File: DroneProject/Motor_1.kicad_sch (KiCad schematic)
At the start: 0 parts

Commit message: Added a second MCU for motor control.  Removed 5V rail.  Added COM switching for SWD and UART external headers
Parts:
- added C1: 10uF, Capacitor_SMD:C_1206_3216Metric, symbol Device:C
- added C2, C3: 0.1uF, Capacitor_SMD:C_0402_1005Metric, symbol Device:C
- added C4, C81: 1uF, Capacitor_SMD:C_0402_1005Metric, symbol Device:C
- added C82: 47nF, Capacitor_SMD:C_0402_1005Metric, symbol Device:C
- added U91: DRV8323SRTAR, Library:RTA0040B, symbol Global:DRV8323SRTAR
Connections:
- new net: C82.1, U91.1 (CPL)
- new net: C82.2, U91.2 (CPH)
- new net: C81.2, U91.3 (VCP)
- new net GND: C3.2, C4.2, U91.32 (AGND), U91.41 (PAD)
- new net GNDPWR: C1.2, C2.2
- new net VCC: C3.1, C4.1, U91.24 (VREF), U91.33 (DVDD)
- new net VDD: C1.1, C2.1, C81.1, U91.4 (VM)

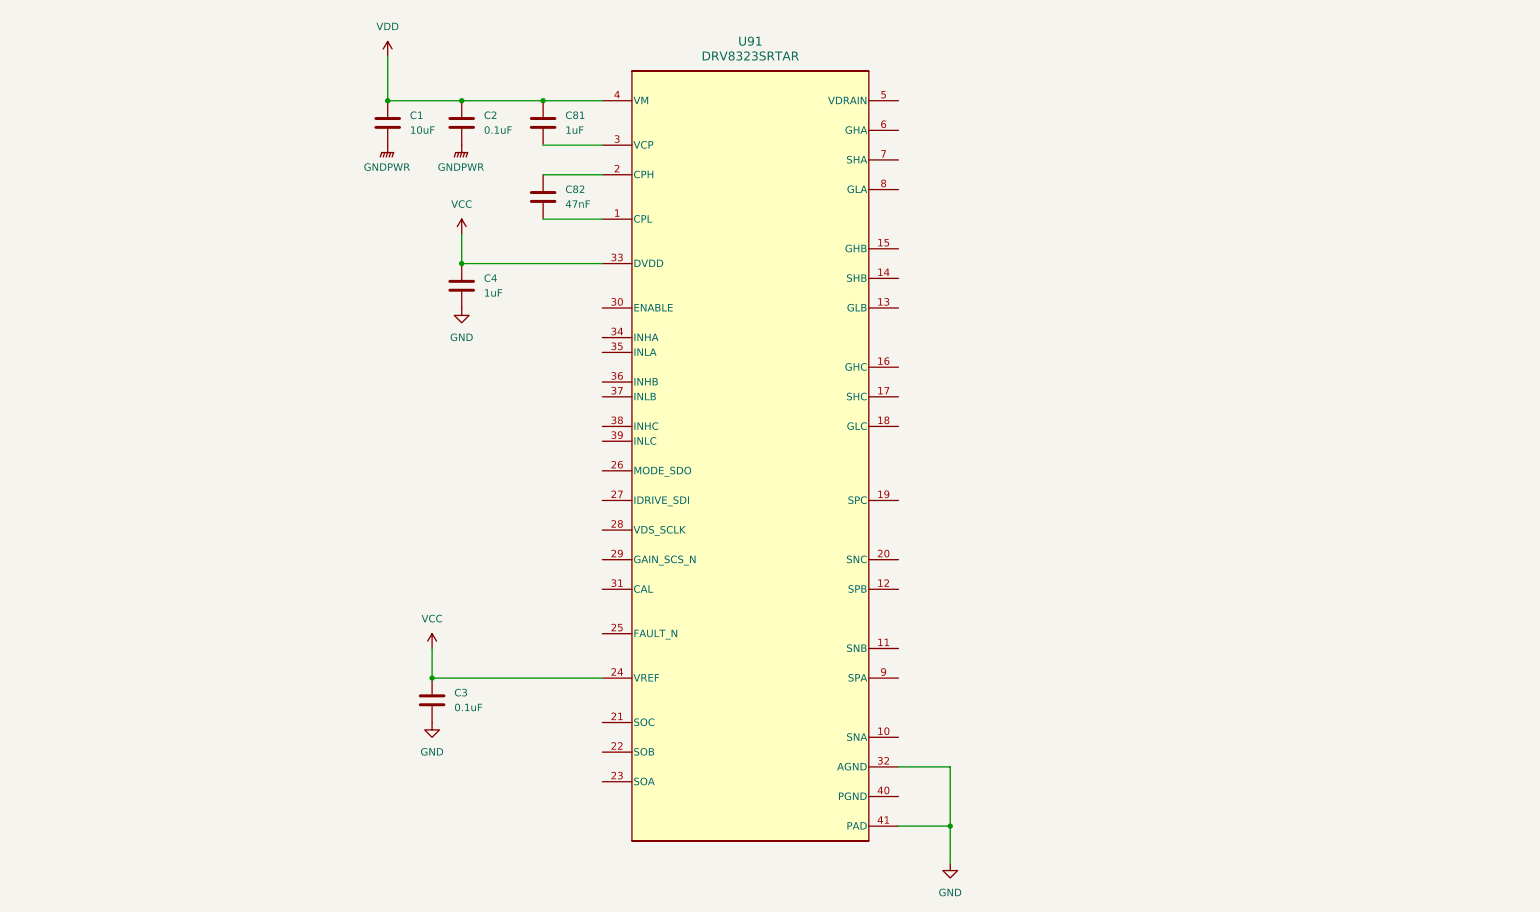
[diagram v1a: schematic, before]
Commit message: Finished motor and C1 designs, still need to rename components on MTR2, 3, and 4 pages
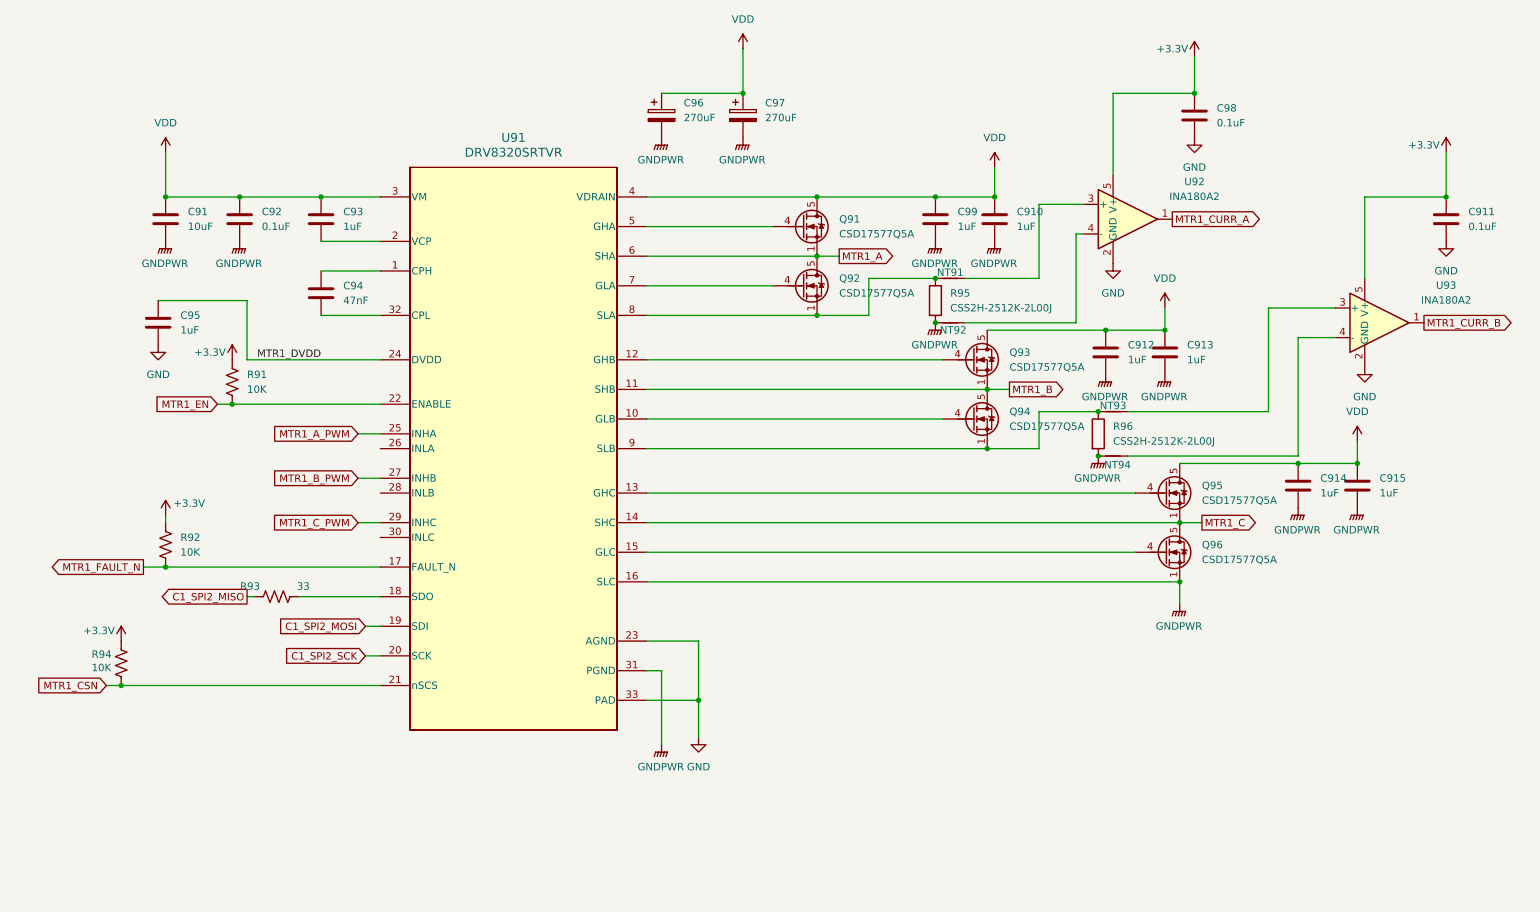
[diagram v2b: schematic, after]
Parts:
- removed C3: 0.1uF, Capacitor_SMD:C_0402_1005Metric, symbol Device:C
- removed U91: DRV8323SRTAR, Library:RTA0040B, symbol Global:DRV8323SRTAR
- added C910, C912, C913, C914, C915, C99: 1uF, Capacitor_SMD:C_0603_1608Metric, symbol Device:C
- added C911, C98: 0.1uF, Capacitor_SMD:C_0402_1005Metric, symbol Device:C
- added C96, C97: 270uF, Capacitor_SMD:CP_Elec_10x10.5, symbol Device:C_Polarized
- added NT91, NT92, NT93, NT94: NetTie_2, NetTie:NetTie-2_SMD_Pad0.5mm, symbol Device:NetTie_2
- added Q91, Q92, Q93, Q94, Q95, Q96: CSD17577Q5A, Package_TO_SOT_SMD:TDSON-8-1, symbol Transistor_FET:CSD17577Q5A
- added R91, R92, R94: 10K, Resistor_SMD:R_0402_1005Metric, symbol Device:R_US
- added R93: 33, Resistor_SMD:R_0402_1005Metric, symbol Device:R_US
- added R95, R96: CSS2H-2512K-2L00J, Resistor_SMD:R_2512_6332Metric, symbol Device:R
- added U91: DRV8320SRTVR, Library:DRV8320SRTVR, symbol Global:DRV8320SRTVR
- added U92, U93: INA180A2, Package_TO_SOT_SMD:SOT-23-5, symbol Amplifier_Current:INA180A2
- renumbered C1 to C91, C2 to C92, C81 to C93, C82 to C94, C4 to C95
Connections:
- net GND: now also C911.2, C98.2, U91.23 (AGND), U91.33 (PAD), U92.2 (GND), U93.2 (GND)
- net GNDPWR: now also C910.2, C912.2, C913.2, C914.2, C915.2, C96.2, C97.2, C99.2, NT92.1, NT94.1, Q96.1 (S), Q96.2 (S), Q96.3 (S), R95.2, R96.2, U91.16 (SLC), U91.31 (PGND)
- net VDD: now also C910.1, C912.1, C913.1, C914.1, C915.1, C96.1, C97.1, C99.1, Q91.5 (D), Q93.5 (D), Q95.5 (D), U91.3 (VM), U91.4 (VDRAIN)
- net at C94.1: now also U91.32 (CPL)
- net at C94.2: now also U91.1 (CPH)
- net at C93.2: now also U91.2 (VCP)
- net VCC renamed MTR1_DVDD
- net MTR1_DVDD: now also U91.24 (DVDD)
- new net: NT93.2, U93.3 (+)
- new net: NT94.2, U93.4 (-)
- new net: Q96.4 (G), U91.15 (GLC)
- new net: NT91.1, Q92.1 (S), Q92.2 (S), Q92.3 (S), R95.1, U91.8 (SLA)
- new net: Q92.4 (G), U91.7 (GLA)
- new net: NT91.2, U92.3 (+)
- new net: Q91.4 (G), U91.5 (GHA)
- new net: R93.2, U91.18 (SDO)
- new net: Q94.4 (G), U91.10 (GLB)
- new net: Q93.4 (G), U91.12 (GHB)
- new net: Q95.4 (G), U91.13 (GHC)
- new net: NT93.1, Q94.1 (S), Q94.2 (S), Q94.3 (S), R96.1, U91.9 (SLB)
- new net: NT92.2, U92.4 (-)
- new net +3.3V: C911.1, C98.1, R91.2, R92.2, R94.2, U92.5 (V+), U93.5 (V+)
- new net C1_SPI2_MISO: R93.1
- new net C1_SPI2_MOSI: U91.19 (SDI)
- new net C1_SPI2_SCK: U91.20 (SCK)
- new net MTR1_A: Q91.1 (S), Q91.2 (S), Q91.3 (S), Q92.5 (D), U91.6 (SHA)
- new net MTR1_A_PWM: U91.25 (INHA)
- new net MTR1_B: Q93.1 (S), Q93.2 (S), Q93.3 (S), Q94.5 (D), U91.11 (SHB)
- new net MTR1_B_PWM: U91.27 (INHB)
- new net MTR1_C: Q95.1 (S), Q95.2 (S), Q95.3 (S), Q96.5 (D), U91.14 (SHC)
- new net MTR1_CSN: R94.1, U91.21 (nSCS)
- new net MTR1_CURR_A: U92.1
- new net MTR1_CURR_B: U93.1
- new net MTR1_C_PWM: U91.29 (INHC)
- new net MTR1_EN: R91.1, U91.22 (ENABLE)
- new net MTR1_FAULT_N: R92.1, U91.17 (FAULT_N)
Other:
- moved on the sheet: C91, C92, C93, C94, C95

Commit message: Finished most of routing for motor controls, however likely going to revert back and make separate ESC boards for motor control as I think that would honestly be more efficient from both a cost and debug complexity standpoint.
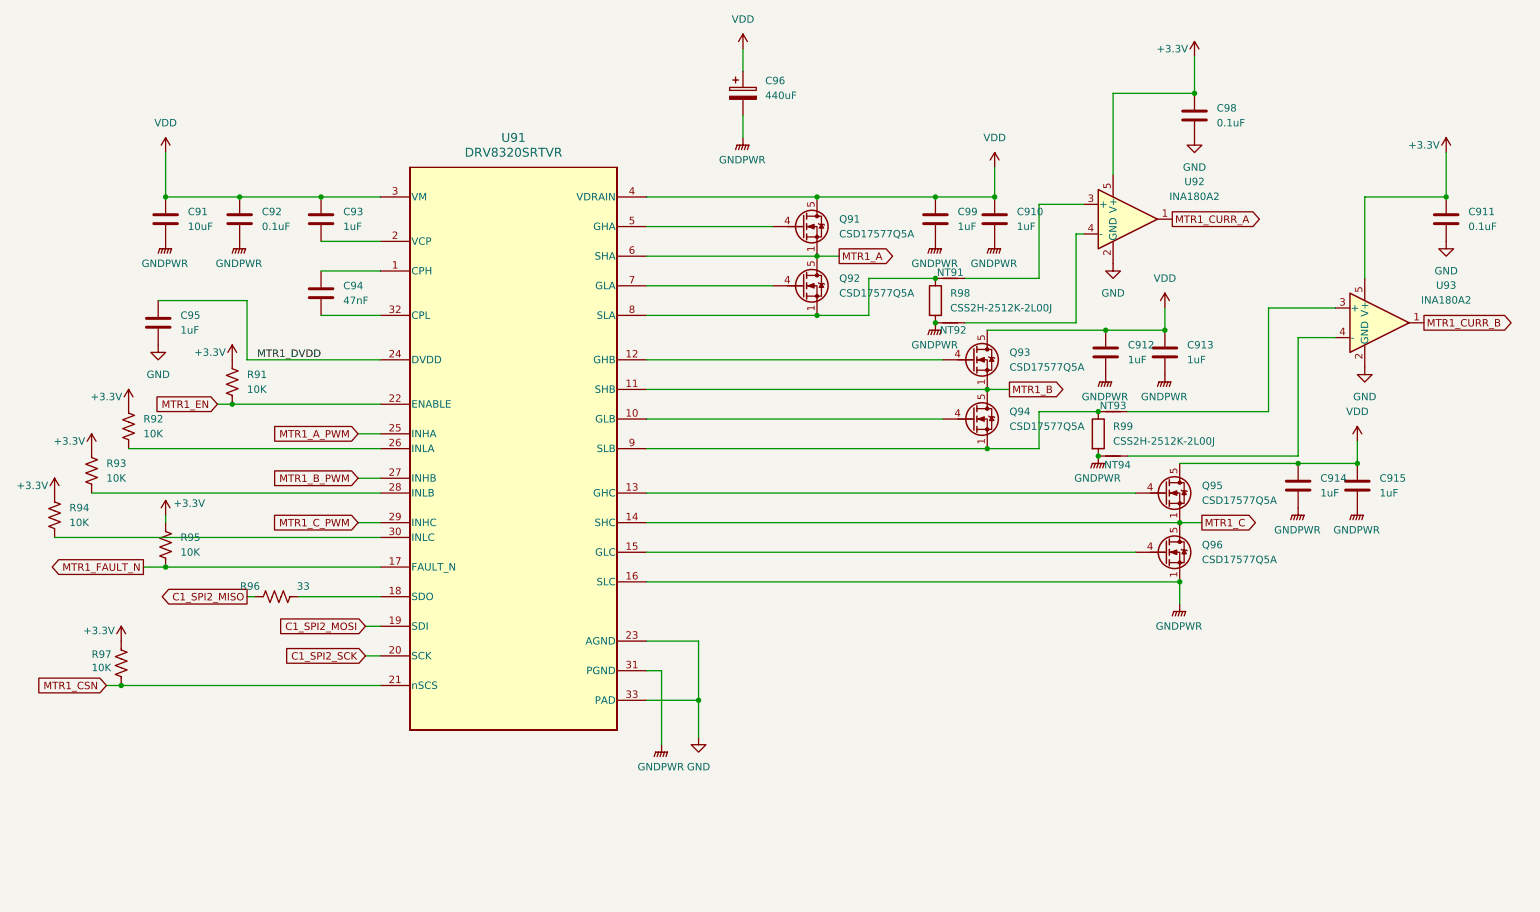
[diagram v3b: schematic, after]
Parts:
- removed C97: 270uF, Capacitor_SMD:CP_Elec_10x10.5, symbol Device:C_Polarized
- added R92, R93, R94: 10K, Resistor_SMD:R_0402_1005Metric, symbol Device:R_US
- C96: value 270uF -> 440uF; footprint Capacitor_SMD:CP_Elec_10x10.5 -> Capacitor_THT:CP_Radial_D10.0mm_P5.00mm
- renumbered R92 to R95, R93 to R96, R94 to R97, R95 to R98, R96 to R99
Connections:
- net +3.3V: now also R92.2, R93.2, R94.2
- net at U91.26 (INLA): now also R92.1
- net at U91.28 (INLB): now also R93.1
- net at U91.30 (INLC): now also R94.1
